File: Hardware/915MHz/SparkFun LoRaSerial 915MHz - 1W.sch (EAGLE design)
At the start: 72 parts, among them J1 QWIIC_RIGHT_ANGLE, J3 USB C, J4 JTAG, Q1 20V/0.2A/8MHz/1.2Ω/1Vth, Q2 20V/0.2A/8MHz/1.2Ω/1Vth, U2 ATSAMD21G-A, U3 AP2112K-3.3, U4 E19-915M30S, Y1 32.768kHz

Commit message: Adjust 50ohm microstrip for four layer
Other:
- note added: "Dielectric thickness (layer 1 to 2): 0.2mm"
- note added: "Er: 4.6 - JLC7628"
- note added: "Polygon Isolation: 10mil/0.254mm"
- note added: "RF Trace Width: 14.2mil/0.36mm"
- note removed: "Dielectric thickness: 1.53mm"
- note removed: "Er: 4.5"
- note removed: "Polygon Isolation: 4mil/0.1016mm"
- note removed: "RF Trace Width: 29.1mil/0.74mm"
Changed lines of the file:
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@@
 &gt;= 5V Ensures Max Output Power</text>
 <text x="45.72" y="175.26" size="1.27" layer="97">Board thickness: 1.6mm</text>
-<text x="45.72" y="170.18" size="1.27" layer="97">Er: 4.5</text>
+<text x="45.72" y="170.18" size="1.27" layer="97">Er: 4.6 - JLC7628</text>
 <text x="45.72" y="177.8" size="1.27" layer="97">Copper Thickness (1oz): 1.4mil/0.035mm</text>
-<text x="45.72" y="165.1" size="1.27" layer="97">RF Trace Width: 29.1mil/0.74mm</text>
-<text x="45.72" y="167.64" size="1.27" layer="97">Polygon Isolation: 4mil/0.1016mm</text>
-<text x="45.72" y="172.72" size="1.27" layer="97">Dielectric thickness: 1.53mm</text>
+<text x="45.72" y="165.1" size="1.27" layer="97">RF Trace Width: 14.2mil/0.36mm</text>
+<text x="45.72" y="167.64" size="1.27" layer="97">Polygon Isolation: 10mil/0.254mm</text>
+<text x="45.72" y="172.72" size="1.27" layer="97">Dielectric thickness (layer 1 to 2): 0.2mm</text>
 <text x="45.72" y="162.56" size="0.762" layer="97">https://chemandy.com/calculators/coplanar-waveguide-with-ground-calculator.htm</text>
 <text x="45.72" y="180.34" size="1.524" layer="97" ratio="15">Waveguide Calculation:</text>

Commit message: Update resistors to increase LED brightness
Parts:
- R12: value 4.7k -> 330; device SparkFun-Resistors:4.7KOHM-0603-1/10W-1% -> SparkFun-Resistors:330OHM-0603-1/10W-1%
- R20, R21, R22, R9: value 4.7k -> 0; device SparkFun-Resistors:4.7KOHM-0603-1/10W-1% -> SparkFun-Resistors:0OHM-0603-1/10W
- R5: value 1k -> 0; device SparkFun-Resistors:1KOHM-0603-1/10W-1% -> SparkFun-Resistors:0OHM-0603-1/10W
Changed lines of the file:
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@@
 <part name="GND3" library="SparkFun-PowerSymbols" deviceset="GND" device=""/>
 <part name="D3" library="SparkFun-LED" deviceset="LED-YELLOW" device="0603" value="Yellow"/>
-<part name="R12" library="SparkFun-Resistors" deviceset="4.7KOHM" device="-0603-1/10W-1%" value="4.7k"/>
-<part name="R5" library="SparkFun-Resistors" deviceset="1KOHM" device="-0603-1/10W-1%" value="1k"/>
+<part name="R12" library="SparkFun-Resistors" deviceset="330OHM" device="-0603-1/10W-1%" value="330"/>
+<part name="R5" library="SparkFun-Resistors" deviceset="0OHM" device="-0603-1/10W" value="0"/>
 <part name="D2" library="SparkFun-LED" deviceset="LED-BLUE" device="0603" value="BLUE"/>
 <part name="J3" library="USB-C" deviceset="USB_C" device="16PIN" value="USB C"/>
@@
 <part name="D5" library="SparkFun-LED" deviceset="LED-RED" device="0603" value="RED"/>
 <part name="R1" library="SparkFun-Resistors" deviceset="1KOHM" device="-0603-1/10W-1%" value="1k"/>
-<part name="R9" library="SparkFun-Resistors" deviceset="4.7KOHM" device="-0603-1/10W-1%" value="4.7k"/>
+<part name="R9" library="SparkFun-Resistors" deviceset="0OHM" device="-0603-1/10W" value="0"/>
 <part name="GND10" library="SparkFun-PowerSymbols" deviceset="GND" device=""/>
 <part name="GND16" library="SparkFun-PowerSymbols" deviceset="GND" device=""/>
@@
 <part name="SUPPLY10" library="SparkFun-PowerSymbols" deviceset="5V" device=""/>
 <part name="SUPPLY14" library="SparkFun-PowerSymbols" deviceset="5V" device=""/>
-<part name="R20" library="SparkFun-Resistors" deviceset="4.7KOHM" device="-0603-1/10W-1%" value="4.7k"/>
+<part name="R20" library="SparkFun-Resistors" deviceset="0OHM" device="-0603-1/10W" value="0"/>
 <part name="D1" library="SparkFun-LED" deviceset="LED-GREEN" device="0603" value="GREEN"/>
 <part name="GND14" library="SparkFun-PowerSymbols" deviceset="GND" device=""/>
-<part name="R21" library="SparkFun-Resistors" deviceset="4.7KOHM" device="-0603-1/10W-1%" value="4.7k"/>
+<part name="R21" library="SparkFun-Resistors" deviceset="0OHM" device="-0603-1/10W" value="0"/>
 <part name="D7" library="SparkFun-LED" deviceset="LED-GREEN" device="0603" value="GREEN"/>
 <part name="GND15" library="SparkFun-PowerSymbols" deviceset="GND" device=""/>
 <part name="D8" library="SparkFun-LED" deviceset="LED-GREEN" device="0603" value="GREEN"/>
-<part name="R22" library="SparkFun-Resistors" deviceset="4.7KOHM" device="-0603-1/10W-1%" value="4.7k"/>
+<part name="R22" library="SparkFun-Resistors" deviceset="0OHM" device="-0603-1/10W" value="0"/>
 <part name="GND26" library="SparkFun-PowerSymbols" deviceset="GND" device=""/>
 <part name="SUPPLY18" library="SparkFun-PowerSymbols" deviceset="3.3V" device=""/>

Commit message: Add RSSI LED drivers. v13
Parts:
- added Q3, Q4, Q5, Q6: 600mA/40V, SparkFun-DiscreteSemi:TRANS_NPN-MMBT2222AL
- added R23, R24, R25, R26: 1k, SparkFun-Resistors:1KOHM-0603-1/10W-1%
- LOGO5: value SFE_LOGO_NAME_FLAME10_MM -> SFE_LOGO_NAME9_MM; device SparkFun-Aesthetics:SFE_LOGO_NAME_FLAME10_MM -> SparkFun-Aesthetics:SFE_LOGO_NAME9_MM
- R20, R21, R22, R9: value 0 -> 220; device SparkFun-Resistors:0OHM-0603-1/10W -> SparkFun-Resistors:220OHM-0603-1/10W-1%
- U4: device SparkFun-RF:E19-915MS1W -> SparkFun-RF:LORA-E19915MHZ
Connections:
- new net N$12: Q3.C, R20.1
- new net N$13: Q3.B, R23.1
- new net N$14: Q4.C, R9.1
- new net N$15: Q4.B, R24.1
- new net N$16: Q5.C, R21.1
- new net N$17: Q5.B, R25.1
- new net N$18: Q6.C, R22.1
- new net N$19: Q6.B, R26.1
- net 3.3V: now also D1.A, D4.A, D7.A, D8.A
- net A3/RSSI1: now also R23.2; no longer D1.A
- net A4/RSSI2: now also R24.2; no longer D4.A
- net D8/RSSI3: now also R25.2; no longer D7.A
- net D9/RSSI4: now also R26.2; no longer D8.A
- net GND: now also Q3.E, Q4.E, Q5.E, Q6.E; no longer R20.1, R21.1, R22.1, R9.1
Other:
- note added: "Buttons, ID, and LEDs"
- note added: "RSSI LEDs"
- note added: "v13"
- note removed: "Buttons, LEDs, ID"
- note removed: "v10"
- moved on the sheet: C12, C13, C14, C15, C16, C19, D1, D2, D3, D4, D5, D7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

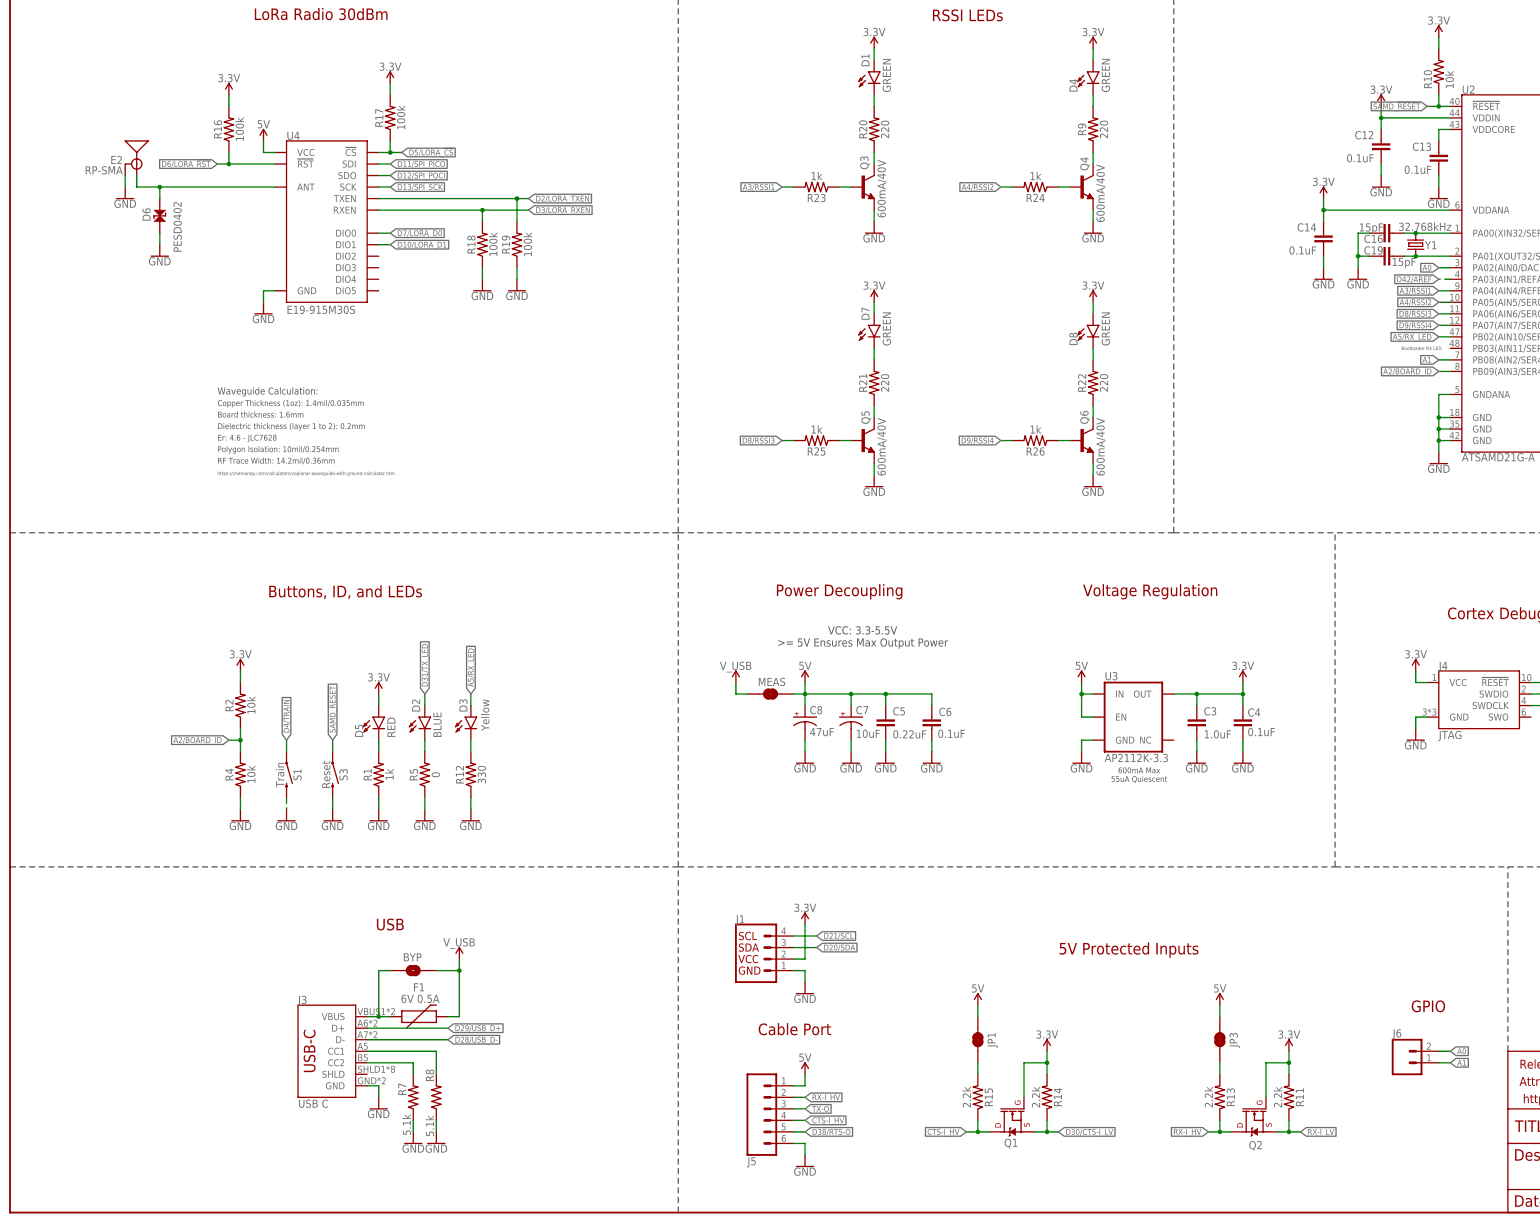
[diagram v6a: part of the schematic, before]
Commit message: Add TPs, GND stitching, sch cosmetic cleanup.
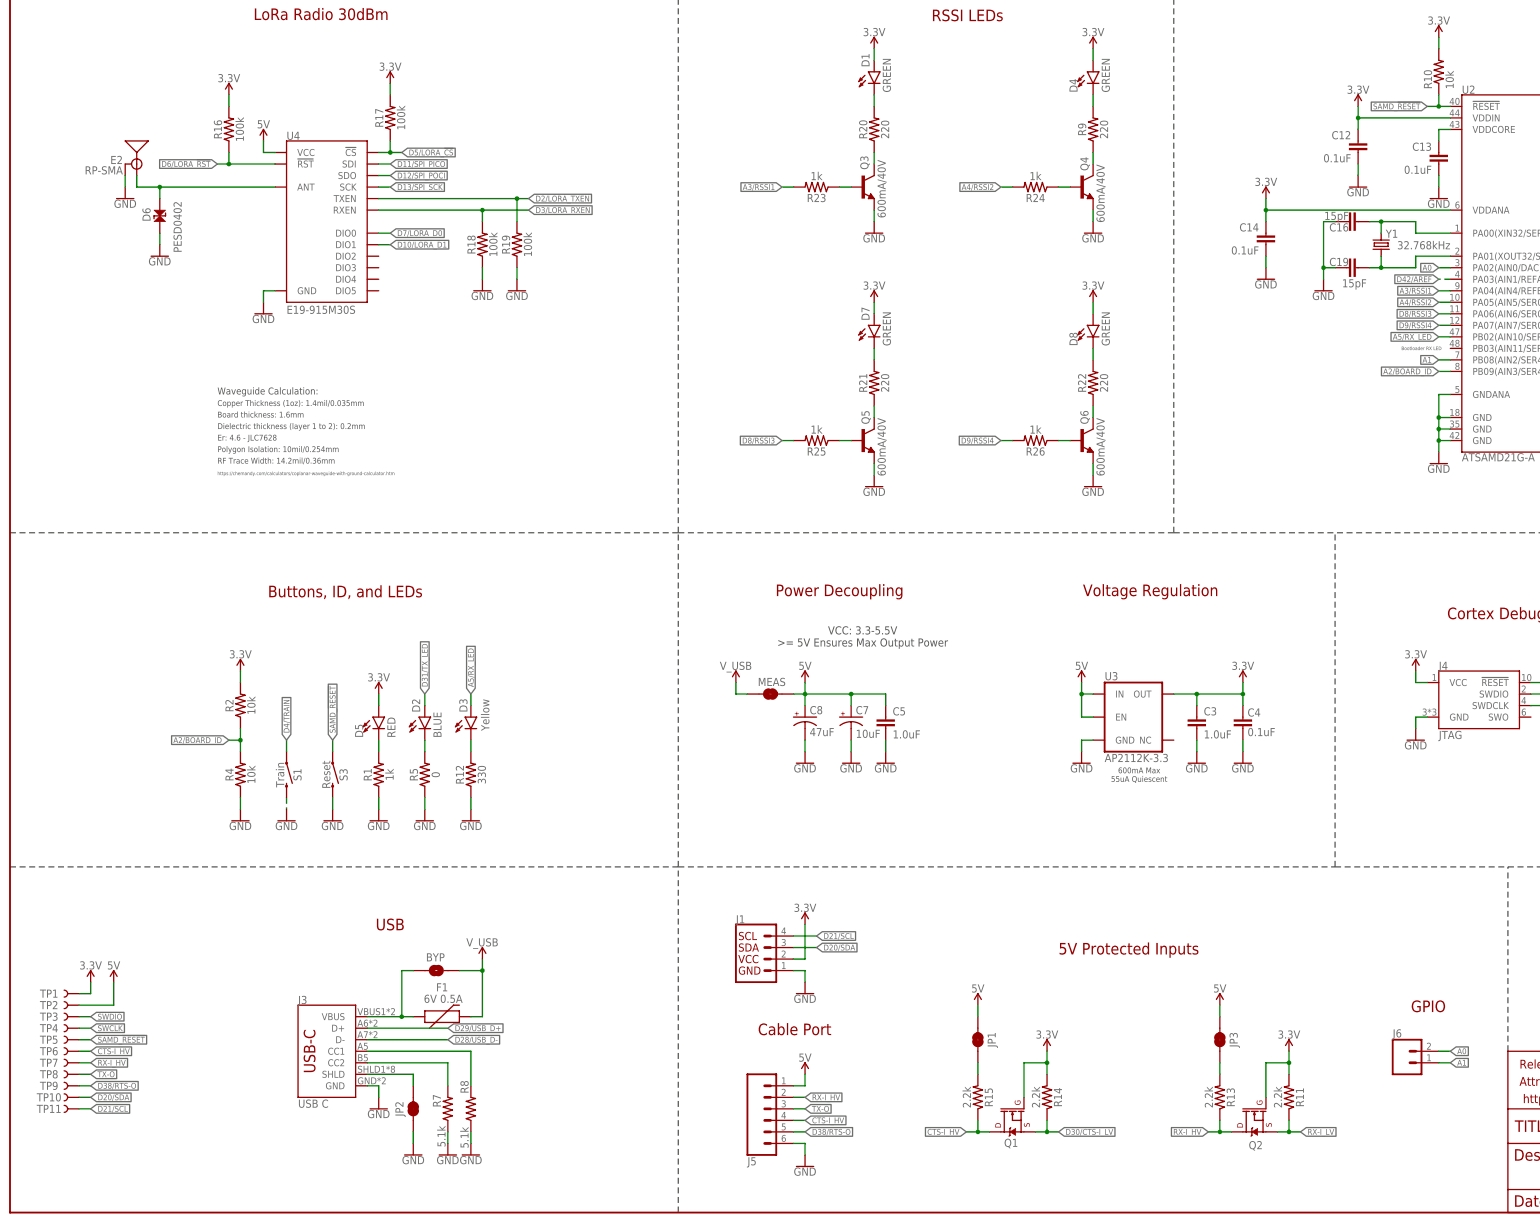
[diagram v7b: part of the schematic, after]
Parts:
- removed C6: 0.1uF, SparkFun-Capacitors:0.1UF-0603-25V-(+80/-20%)
- added JP2: JUMPER-SMT_2_NC_TRACE_SILK, SparkFun-Jumpers:JUMPER-SMT_2_NC_TRACE_SILK
- added TP1, TP10, TP11, TP2, TP3, TP4, TP5, TP6, TP7, TP8, TP9: TEST-POINT3X5, SparkFun-Connectors:TEST-POINT3X5
- C5: value 0.22uF -> 1.0uF; device SparkFun-Capacitors:0.22UF-0603-25V-10% -> SparkFun-Capacitors:1.0UF-0603-16V-10%-X7R
- LOGO2: value SFE_LOGO_NAME_FLAME.1_INCH -> SFE_LOGO_NAME_FLAME9_MM; device SparkFun-Aesthetics:SFE_LOGO_NAME_FLAME.1_INCH -> SparkFun-Aesthetics:SFE_LOGO_NAME_FLAME9_MM
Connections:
- new net N$20: J3.SHLD, JP2.2
- net 3.3V: now also TP1.1
- net 5V: now also TP2.1; no longer C6.1
- net CTS-I_HV: now also TP6.1
- net D20/SDA: now also TP10.1
- net D21/SCL: now also TP11.1
- net D38/RTS-O: now also TP9.1
- net GND: now also JP2.1; no longer C6.2
- net RX-I_HV: now also TP7.1
- net SAMD_!RESET!: now also TP5.1
- net SWCLK: now also TP4.1
- net SWDIO: now also TP3.1
- net TX-O: now also TP8.1
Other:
- moved on the sheet: BYP, C12, C14, C16, C19, F1, R7, R8, Y1

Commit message: v13 - panel files.
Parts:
- removed BYP: JUMPER-SMT_2_NO_SILK, SparkFun-Jumpers:JUMPER-SMT_2_NO_SILK
- removed MEAS: JUMPER-COMBO_2_NC_TRACE, SparkFun-Jumpers:JUMPER-COMBO_2_NC_TRACE
- added D9: 3A/10V/280mV, SparkFun-DiscreteSemi:DIODE-SCHOTTKY-BAT60A
- added Q7: (no value), SparkFun-DiscreteSemi:TRANS_PNP_DUALSOT-363
- added Q8: 20V/4.2A/52mΩ/1.4W, SparkFun-DiscreteSemi:MOSFET_PCH-DMG2305UX-7
- added R27: 100k, SparkFun-Resistors:100KOHM-0603-1/10W-1%
- added R28: 1M, SparkFun-Resistors:1MOHM-0603-1/4W-5%
- added TP12, TP13: TEST-POINT3X5, SparkFun-Connectors:TEST-POINT3X5
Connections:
- new net N$21: Q7G2.C, Q8.G, R28.2
- new net N$22: Q7G1.B, Q7G1.C, Q7G2.B, R27.2
- new net VCC_CABLE: J5.1, Q7G1.E, Q8.D
- net 5V: now also D9.C, Q7G2.E, Q8.S; no longer J5.1, MEAS.2
- net A0: now also TP12.1
- net A1: now also TP13.1
- net GND: now also R27.1, R28.1
- net VUSB: no longer BYP.1
- net V_USB: now also D9.A; no longer BYP.2, MEAS.1
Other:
- note added: "Source Selection"
- note added: "Test Points"
- moved on the sheet: C5, D2, D3, D5, F1, J3, JP2, R1, R12, R2, R4, R5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
